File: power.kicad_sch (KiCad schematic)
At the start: 14 parts, among them IC1 ST1L05CPU33R, U2 LD1117S50TR_SOT223

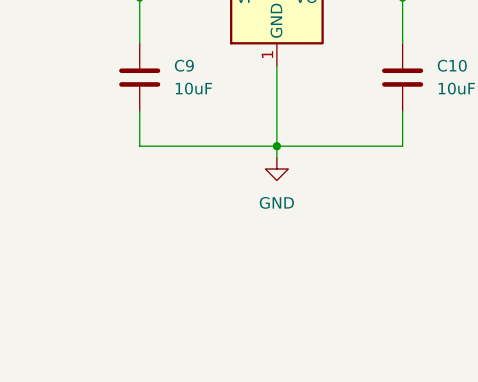
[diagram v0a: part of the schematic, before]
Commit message: Change 0201 to 0403
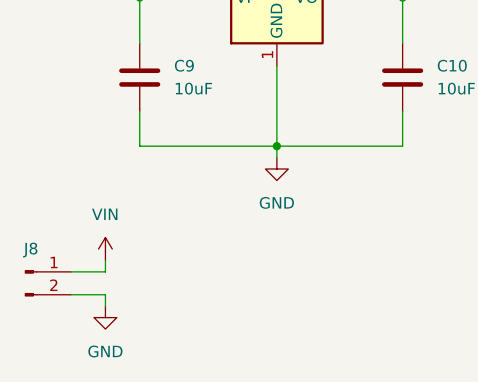
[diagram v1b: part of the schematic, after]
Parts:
- added J8: Conn_01x02_Pin, Connector_PinHeader_2.54mm:PinHeader_1x02_P2.54mm_Vertical, symbol Connector:Conn_01x02_Pin
- C11, C12: footprint Capacitor_SMD:C_0603_1608Metric -> Capacitor_SMD:C_0402_1005Metric
- C3, C4, C5, C6, C7, C8: footprint Capacitor_SMD:C_0201_0603Metric -> Capacitor_SMD:C_0402_1005Metric
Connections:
- net GND: now also J8.2 (Pin_2)
- net VIN: now also J8.1 (Pin_1)

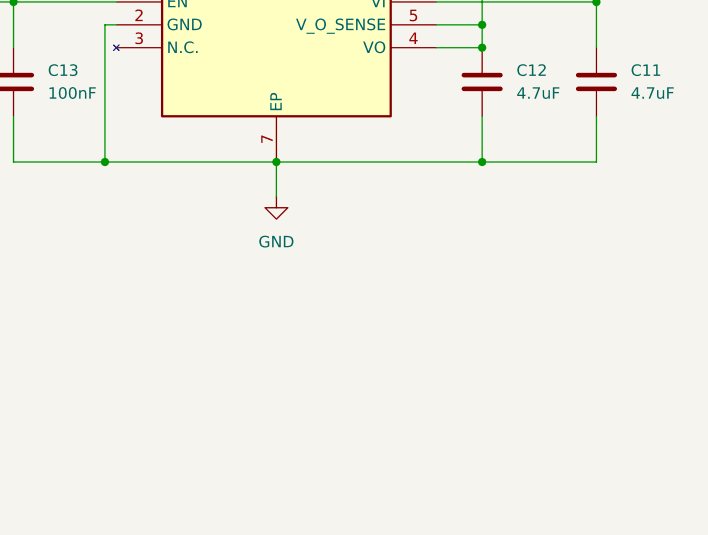
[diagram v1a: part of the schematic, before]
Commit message: Added STM32_MX Project, LED, Fixed DRC Violations
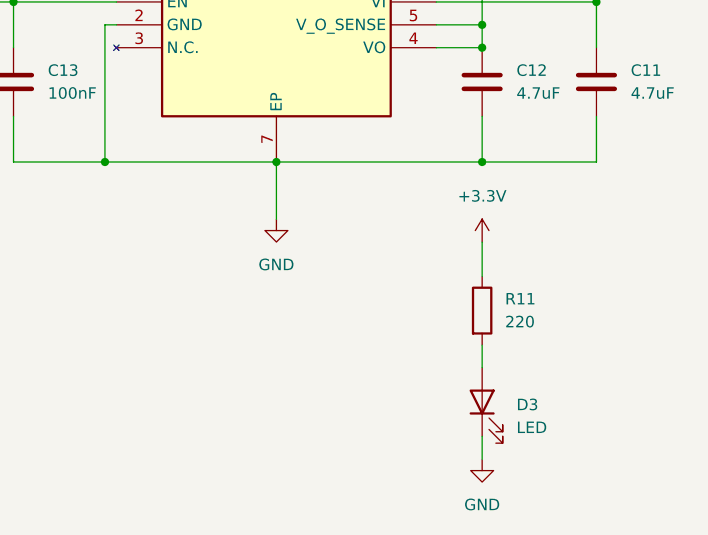
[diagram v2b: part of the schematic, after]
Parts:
- added D3: LED, LED_SMD:LED_0603_1608Metric, symbol Device:LED
- added R11: 220, Resistor_SMD:R_0402_1005Metric, symbol Device:R
- C13: footprint Capacitor_SMD:C_0603_1608Metric -> Capacitor_SMD:C_0402_1005Metric
- IC1: footprint SON95P300X300X100-7N-D -> VanguardLib:SON95P300X300X100-7N-D
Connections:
- net +3.3V: now also R11.1
- net GND: now also D3.1 (K)
- new net: D3.2 (A), R11.2
